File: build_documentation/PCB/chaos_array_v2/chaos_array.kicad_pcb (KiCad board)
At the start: 2 copper layers, 106.4 x 70.9 mm, 181 parts, among them J10 Conn_01x01_Pin, J2 Conn_01x08_Socket, J3 Conn_01x01_Pin, J4 Conn_01x01_Pin, J5 Conn_01x01_Pin, J6 Conn_01x01_Pin, J7 Conn_01x01_Pin, J8 Conn_01x01_Pin, J9 Conn_01x01_Pin, SW1 RotaryEncoder_Switch, SW2 SW_Push, SW3 RotaryEncoder_Switch, SW4 SW_Push, SW5 RotaryEncoder_Switch, SW6 SW_Push, SW7 RotaryEncoder_Switch, SW8 SW_Push, U1 RP2040-Zero

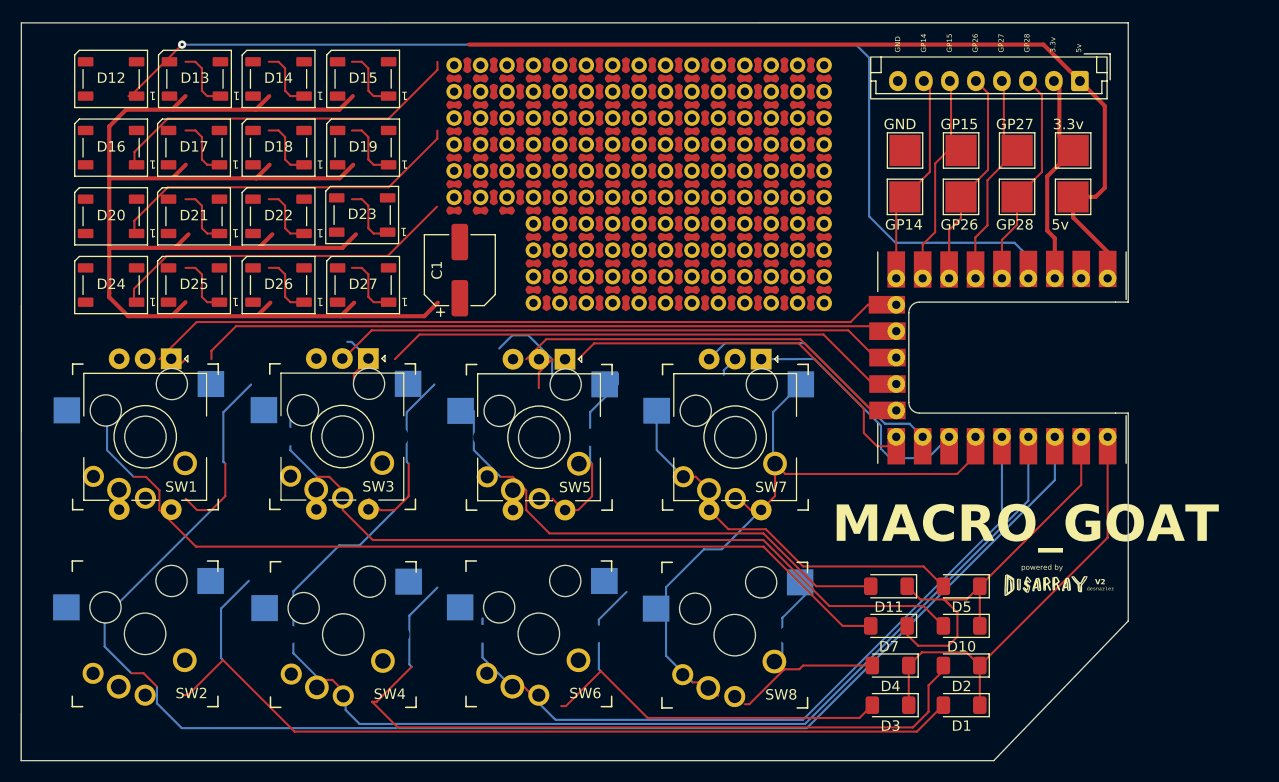
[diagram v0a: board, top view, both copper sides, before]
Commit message: fix_LED_not_grounded
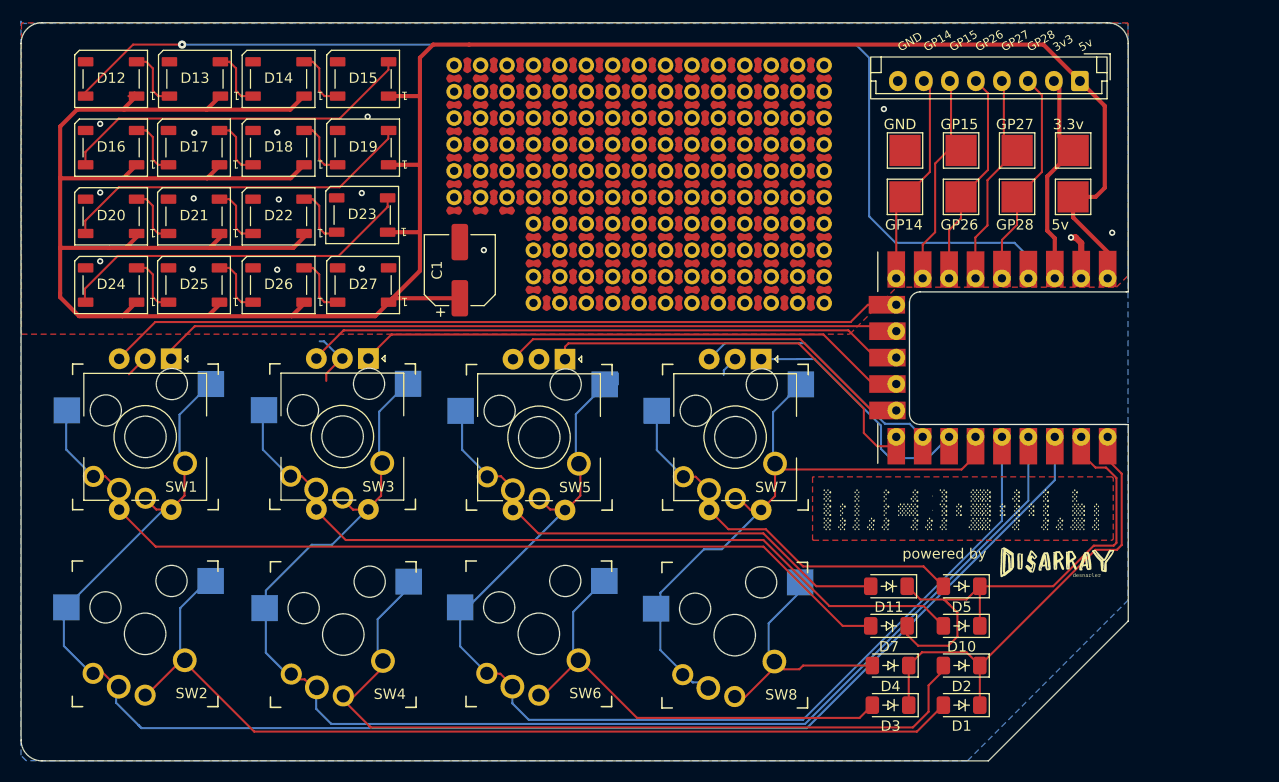
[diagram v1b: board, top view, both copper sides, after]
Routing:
- net +5V: track 324.6 -> 268.6 mm
- net Net-(D23-DOUT): track 0.00 -> 34.5 mm
- net /col_2: track 89.8 -> 107.6 mm
- net /row_0: track 40.7 -> 49.3 mm
- net Net-(D26-DOUT): track 0.00 -> 5.79 mm
- net Net-(D25-DOUT): track 0.00 -> 5.79 mm
- net Net-(D24-DOUT): track 0.00 -> 5.79 mm
- net Net-(D22-DOUT): track 0.00 -> 5.79 mm
- net Net-(D21-DOUT): track 0.00 -> 5.79 mm
- net Net-(D20-DOUT): track 0.00 -> 5.79 mm
- net Net-(D18-DOUT): track 0.00 -> 5.79 mm
- net Net-(D17-DOUT): track 0.00 -> 5.79 mm
- net Net-(D16-DOUT): track 0.00 -> 5.79 mm
- net Net-(D14-DOUT): track 0.00 -> 5.79 mm
- net Net-(D13-DOUT): track 0.00 -> 5.79 mm
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- added copper zone on F.Cu, net (none)
- added copper zone on B.Cu, net GND
- added copper zone on F.Cu, net GND
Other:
- board size 106.4 x 70.9 mm -> 106.4 x 71 mm
- board text added: "3v3"
- board text added: "GP14 - SCK SDA GP15 - TX SCL GP26 - ADC SDL GP27 - ADC SCL GP28 - ADC"
- board text removed: "MACRO_GOAT"
- board text removed: "V2"
